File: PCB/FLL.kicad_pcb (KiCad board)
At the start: 2 copper layers, 9 parts, among them U1 MCP73831-2-MC, U3 LM317L_SOT-89

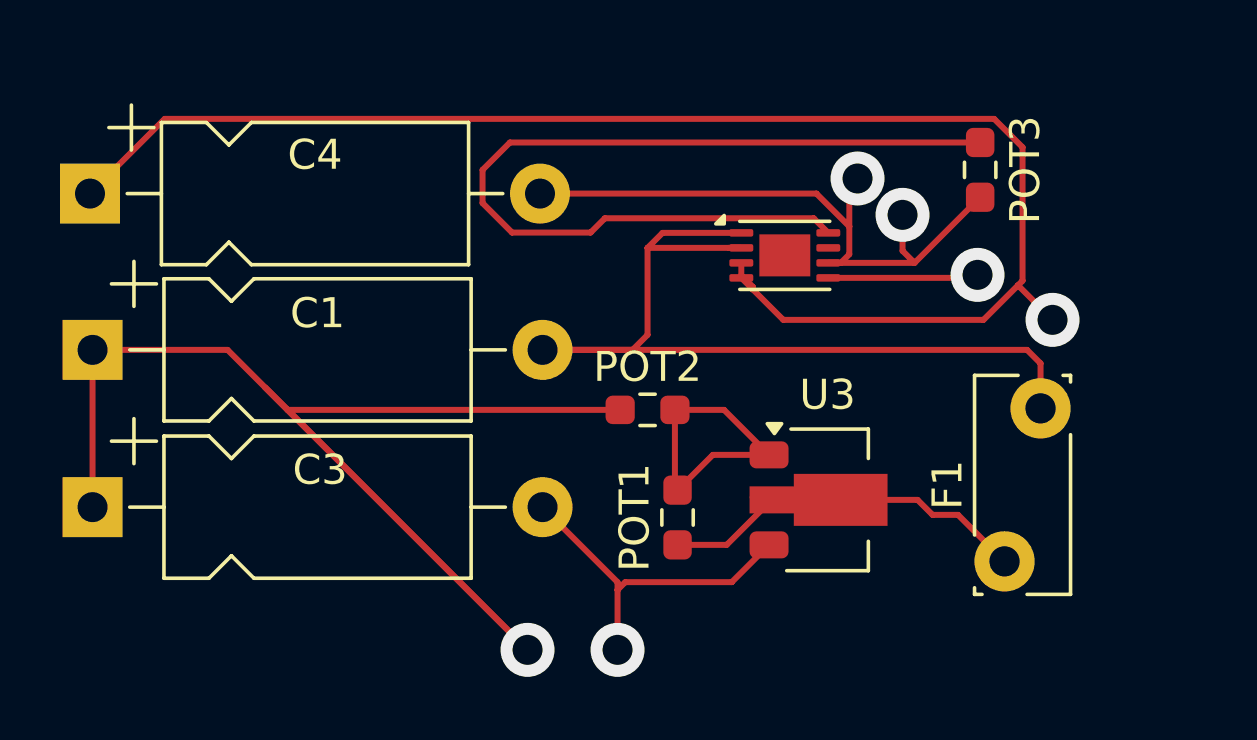
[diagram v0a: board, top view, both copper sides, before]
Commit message: Update PCB design configuration and net colors
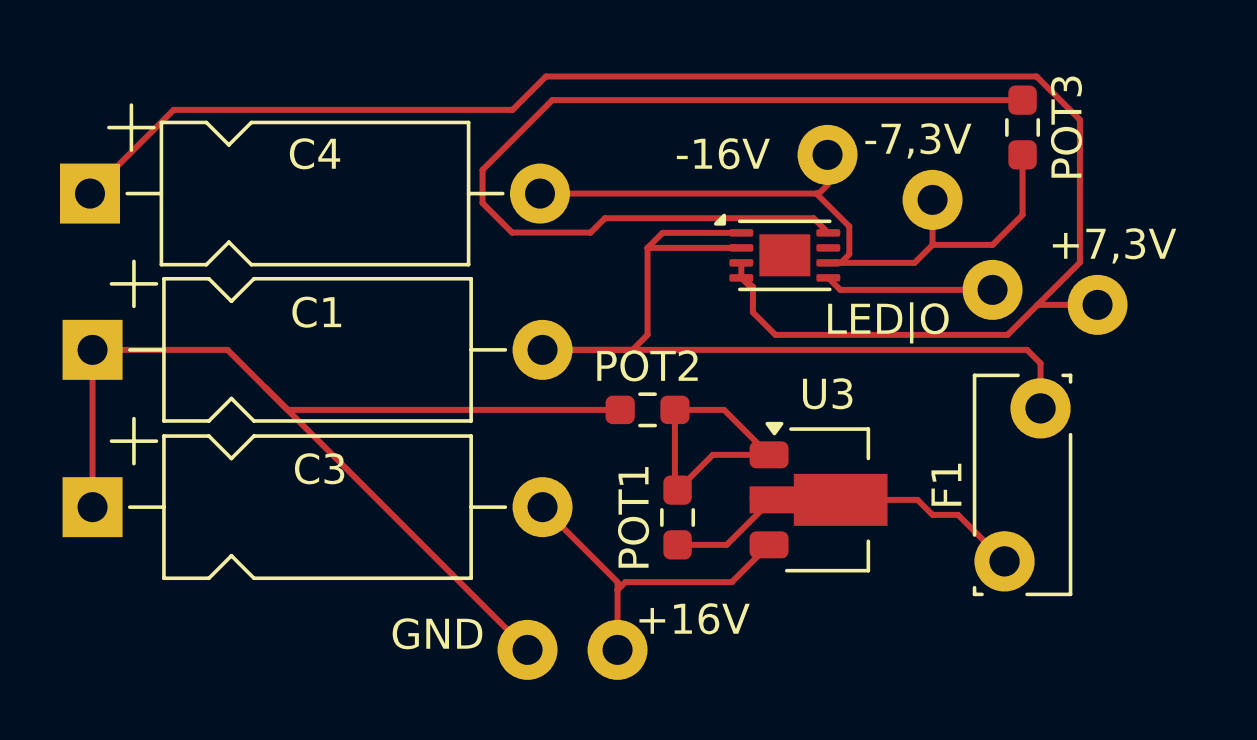
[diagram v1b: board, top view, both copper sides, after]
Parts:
- added ?: , , F.Cu at (170.5, 36.0)
- added ?: , , F.Cu at (160.5, 52.5)
- added ?: , , F.Cu at (176.0, 40.5)
- added ?: , , F.Cu at (163.5, 52.5)
- added ?: , , F.Cu at (174.0, 37.5)
- added ?: , , F.Cu at (179.5, 41.0)
- moved POT3 2.00 mm to (177.0, 35.1)
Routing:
- net GND: track 47.3 -> 36.0 mm, vias 1 -> 0
- net +7.5V: track 50.1 -> 56.5 mm, vias 1 -> 0
- net -16V: track 22.4 -> 25.1 mm, vias 2 -> 0
- net Net-(U1-PROG): track 30.4 -> 32.4 mm
- net +1V0: track 5.02 -> 5.78 mm, vias 1 -> 0
- net +16V: vias 1 -> 0
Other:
- board text added: "+16V"
- board text added: "+7,3V"
- board text added: "-16V"
- board text added: "-7,3V"
- board text added: "GND"
- board text added: "LED|O"

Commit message: chore: Update PCB design configuration and remove unnecessary files
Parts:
- added J1: Jack-DC, Connector_BarrelJack:BarrelJack_CUI_PJ-063AH_Horizontal_CircularHoles, F.Cu at (6.78, 2.52)
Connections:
- ? pad 1: -16V -> -7.5V
- C3 pad 2: +16V -> Net-(U3-VI)
- C4 pad 2: -16V -> -7.5V
- POT3 pad 2: -16V -> -7.5V
- U1 pad 6: -16V -> -7.5V
- U3 pad 3: +16V -> Net-(U3-VI)
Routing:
- net -16V: track 25.1 -> 1.50 mm
- net -7.5V: track 0.00 -> 23.1 mm
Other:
- board text added: "C4"
- board text removed: "${REFERENCE}"

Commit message: chore: Update PCB design configuration and remove unnecessary files
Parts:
- removed J1: Jack-DC, Connector_BarrelJack:BarrelJack_CUI_PJ-063AH_Horizontal_CircularHoles

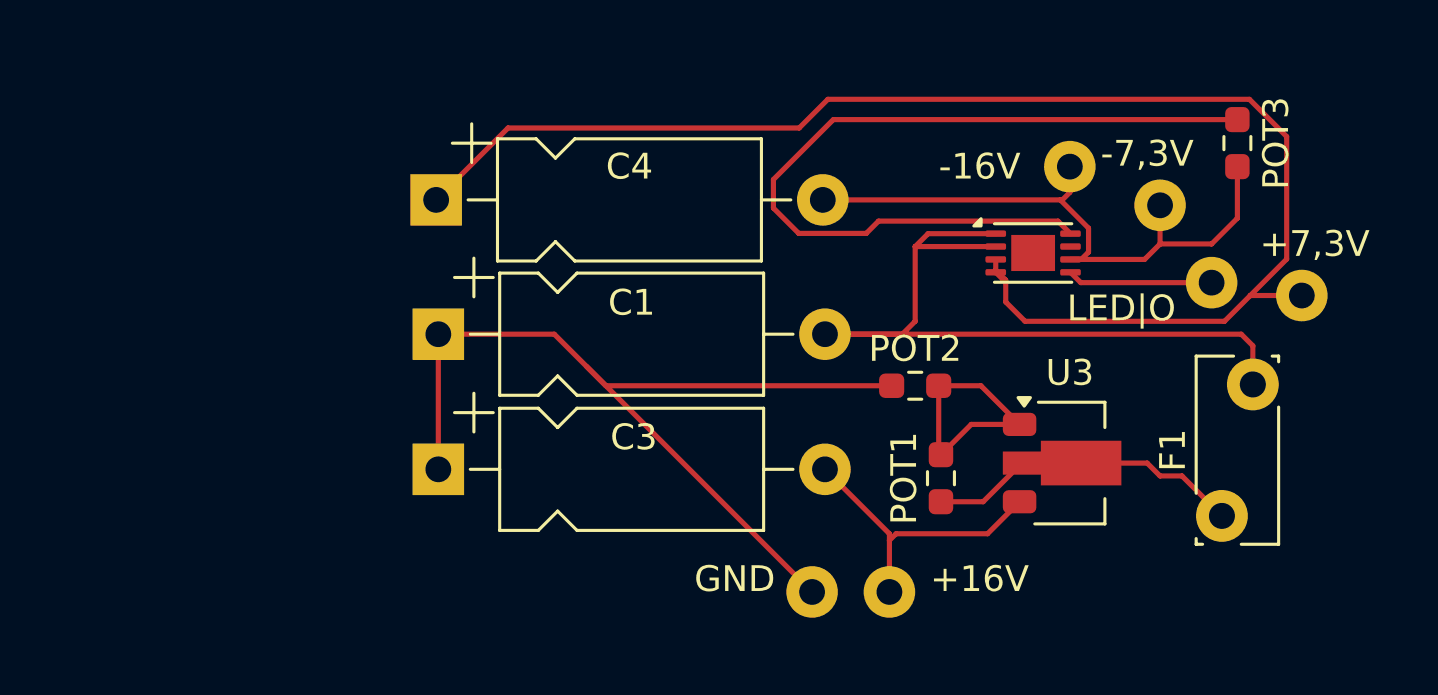
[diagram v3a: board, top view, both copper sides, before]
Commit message: Update PCB design configuration and remove unnecessary files
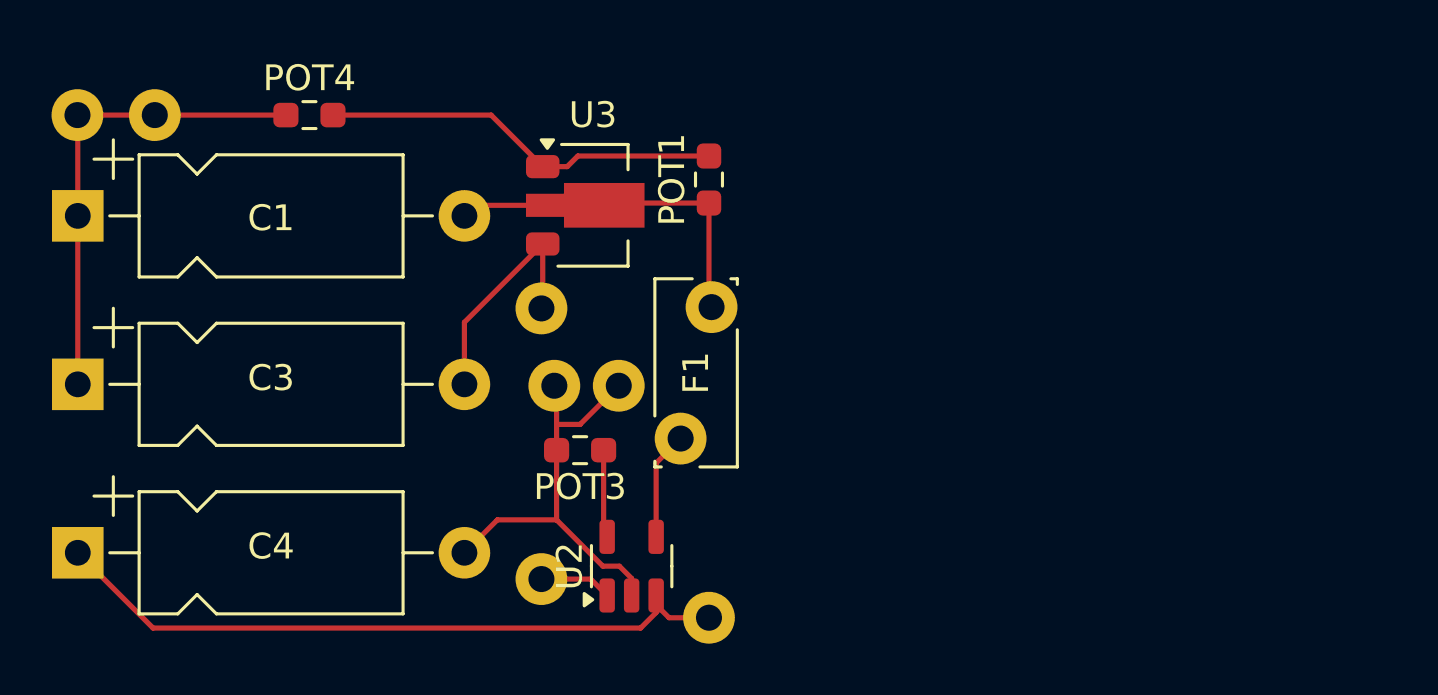
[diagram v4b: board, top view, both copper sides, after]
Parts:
- removed the ? at (170.5, 36.0)
- removed the ? at (160.5, 52.5)
- removed the ? at (176.0, 40.5)
- removed the ? at (163.5, 52.5)
- removed the ? at (174.0, 37.5)
- removed the ? at (179.5, 41.0)
- removed POT2: 1,4kΩ, Resistor_SMD:R_0603_1608Metric_Pad0.98x0.95mm_HandSolder
- removed U1: MCP73831-2-MC, Package_DFN_QFN:DFN-8-1EP_3x2mm_P0.5mm_EP1.7x1.4mm
- added ?: , , F.Cu at (135.0, 34.0)
- added ?: , , F.Cu at (153.0, 44.5)
- added ?: , , F.Cu at (150.5, 44.5)
- added ?: , , F.Cu at (150.0, 41.5)
- added ?: , , F.Cu at (132.0, 34.0)
- added ?: , , F.Cu at (150.0, 52.0)
- added ?: , , F.Cu at (156.5, 53.5)
- added POT4: 1,4kΩ, Resistor_SMD:R_0603_1608Metric_Pad0.98x0.95mm_HandSolder, F.Cu at (141.0, 34.0)
- added U2: MCP73831-2-OT, Package_TO_SOT_SMD:SOT-23-5, F.Cu at (153.5, 51.5)
- moved POT3 28.1 mm to (151.5, 47.0), turned to 180 degrees
- moved F1 21.4 mm to (156.6, 41.5), turned to -90 degrees
- moved U3 21.0 mm to (152.0, 37.5)
- moved C4 19.5 mm to (132.0, 51.0)
- moved C1 14.7 mm to (132.0, 37.9)
- moved POT1 14.7 mm to (156.5, 36.5)
- moved C3 14.4 mm to (132.0, 44.4)
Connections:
- C1 pad 2: Net-(C1-Pad2) -> Net-(U3-VO)
- F1 pad 2: Net-(C1-Pad2) -> Net-(U2-V_{DD})
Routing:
- net Net-(C1-Pad2): track 31.4 -> 0.00 mm
- net +7.5V: track 56.5 -> 27.2 mm
- net Net-(U2-PROG): track 32.4 -> 3.42 mm
- net GND: track 36.0 -> 18.6 mm
- net +16V: track 11.5 -> 0.00 mm
- net Net-(U3-VI): track 0.00 -> 9.22 mm
- net -7.5V: track 23.1 -> 17.4 mm
- net Net-(U3-ADJ): track 10.0 -> 15.6 mm
- net Net-(U2-V_{DD}): track 0.00 -> 4.21 mm
- net +1V0: track 5.64 -> 2.81 mm
- net -16V: track 1.50 -> 0.00 mm
- net Net-(U3-VO): track 12.4 -> 13.8 mm
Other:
- board text removed: "+16V"
- board text removed: "+7,3V"
- board text removed: "-16V"
- board text removed: "-7,3V"
- board text removed: "C4"
- board text removed: "GND"
- board text removed: "LED|O"

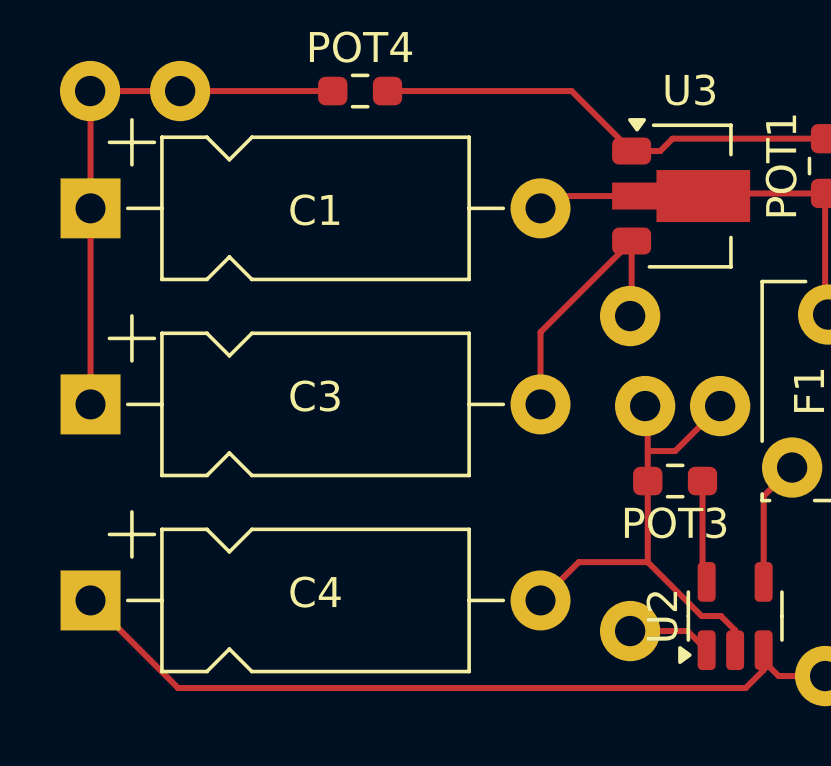
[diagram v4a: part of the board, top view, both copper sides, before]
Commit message: Update PCB design configuration and remove unnecessary files
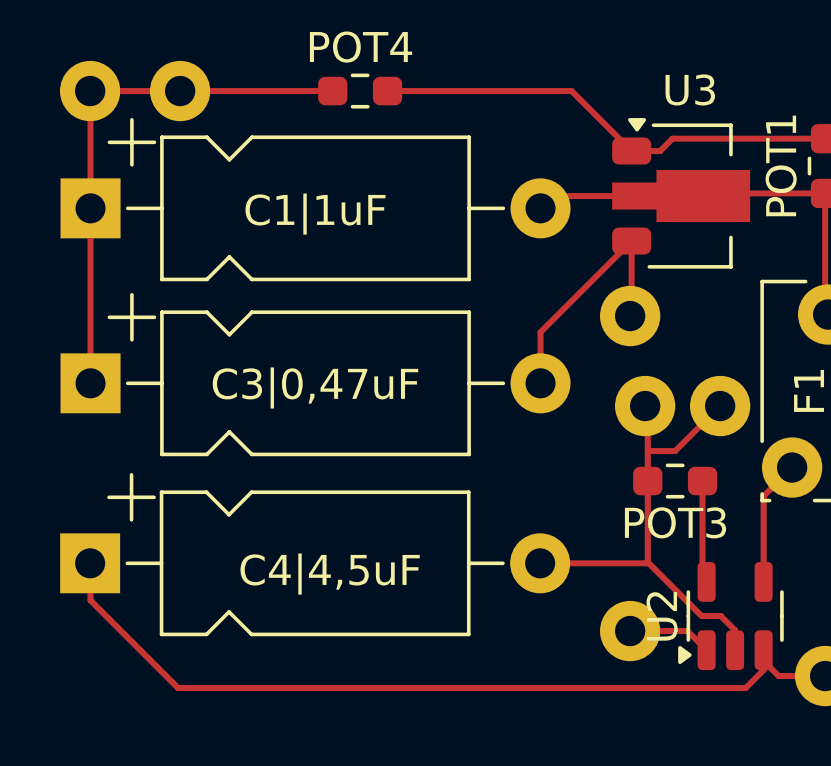
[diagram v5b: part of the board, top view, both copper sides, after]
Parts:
- moved C4|4,5uF 1.24 mm to (132.0, 49.7)
- moved C3|0,47uF 0.70 mm to (132.0, 43.7)
- renumbered C1 to C1|1uF, C3 to C3|0,47uF, C4 to C4|4,5uF
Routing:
- net +7.5V: track 27.2 -> 28.4 mm
- net -7.5V: track 17.4 -> 16.4 mm
- net Net-(U3-VI): track 9.22 -> 8.52 mm
- net GND: track 18.6 -> 17.9 mm
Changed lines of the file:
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@@
 	(footprint "Capacitor_THT:CP_Axial_L10.0mm_D4.5mm_P15.00mm_Horizontal"
 		(layer "F.Cu")
-		(at 132.0125 44.445)
+		(at 132.0125 43.7425)
 		(descr "CP, Axial series, Axial, Horizontal, pin pitch=15mm, , length*diameter=10*4.5mm^2, Electrolytic Capacitor, , http://www.vishay.com/docs/28325/021asm.pdf")
 		(tags "CP Axial series Axial Horizontal pin pitch 15mm  length 10mm diameter 4.5mm Electrolytic Capacitor")
-		(property "Reference" "C3"
-			(at 7.5 -0.2425 0)
+		(property "Reference" "C3|0,47uF"
+			(at 7.5 0.055 0)
 			(layer "F.SilkS")
 			(effects
@@
 			(at 7.9875 1.555 0)
 			(layer "F.Fab")
+			(hide yes)
 			(effects
 				(font
@@
 	(footprint "Capacitor_THT:CP_Axial_L10.0mm_D4.5mm_P15.00mm_Horizontal"
 		(layer "F.Cu")
-		(at 132.0125 50.98)
+		(at 132 49.7425)
 		(descr "CP, Axial series, Axial, Horizontal, pin pitch=15mm, , length*diameter=10*4.5mm^2, Electrolytic Capacitor, , http://www.vishay.com/docs/28325/021asm.pdf")
 		(tags "CP Axial series Axial Horizontal pin pitch 15mm  length 10mm diameter 4.5mm Electrolytic Capacitor")
-		(property "Reference" "C4"
-			(at 7.5 -0.2425 0)
+		(property "Reference" "C4|4,5uF"
+			(at 8 0.2575 0)
 			(layer "F.SilkS")
 			(effects
@@
 			(at 7.9875 1.52 0)
 			(layer "F.Fab")
+			(hide yes)
 			(effects
 				(font
@@
 			(layer "F.Fab")
 		)
-		(fp_text user "${REFERENCE}"
-			(at 7.5 0 0)
-			(layer "F.Fab")
-			(effects
-				(font
-					(size 1 1)
-					(thickness 0.15)
-				)
-			)
-		)
 		(pad "1" thru_hole rect
 			(at 0 0)
@@
 			(at 0 1.43 0)
 			(layer "F.Fab")
+			(hide yes)
 			(effects
 				(font
@@
 		)
 		(property "Value" "MCP73831-2-OT"
-			(at 0 2.4 90)
+			(at 3 5 90)
 			(layer "F.Fab")
+			(hide yes)
 			(effects
 				(font
@@
 		(descr "CP, Axial series, Axial, Horizontal, pin pitch=15mm, , length*diameter=10*4.5mm^2, Electrolytic Capacitor, , http://www.vishay.com/docs/28325/021asm.pdf")
 		(tags "CP Axial series Axial Horizontal pin pitch 15mm  length 10mm diameter 4.5mm Electrolytic Capacitor")
-		(property "Reference" "C1"
+		(property "Reference" "C1|1uF"
 			(at 7.5 0.09 0)
 			(layer "F.SilkS")
@@
 			(at 7.5 1.59 0)
 			(layer "F.Fab")
+			(hide yes)
 			(effects
 				(font
@@
 		)
 		(fp_text user "${REFERENCE}"
-			(at 7.5 0 0)
+			(at 7.4875 0.09 0)
 			(layer "F.Fab")
 			(effects
@@
 	)
 	(segment
-		(start 154.45 52.6375)
-		(end 154.45 53)
+		(start 132.0125 50.98)
+		(end 134.9325 53.9)
 		(width 0.2)
 		(layer "F.Cu")
@@
 	)
 	(segment
-		(start 132.0125 50.98)
-		(end 134.9325 53.9)
+		(start 132.0125 49.7425)
+		(end 132.0125 50.98)
+		(width 0.2)
+		(layer "F.Cu")
+		(net 1)
+	)
+	(segment
+		(start 154.45 52.6375)
+		(end 154.45 53)
 		(width 0.2)
 		(layer "F.Cu")
@@
 	)
 	(segment
-		(start 132.0875 37.835)
-		(end 132.0125 37.91)
+		(start 132.0125 37.91)
+		(end 132.0125 43.7425)
 		(width 0.2)
 		(layer "F.Cu")
@@
 	)
 	(segment
-		(start 132.0125 34.0125)
-		(end 132 34)
+		(start 132.0875 37.835)
+		(end 132.0125 37.91)
 		(width 0.2)
 		(layer "F.Cu")
@@
 	)
 	(segment
-		(start 132.0125 37.91)
-		(end 132.0125 44.445)
+		(start 132.0125 34.0125)
+		(end 132 34)
 		(width 0.2)
 		(layer "F.Cu")
@@
 	)
 	(segment
-		(start 147.0125 44.445)
-		(end 147.0125 42.0375)
+		(start 150.05 41.45)
+		(end 150 41.5)
 		(width 0.2)
 		(layer "F.Cu")
@@
 	)
 	(segment
-		(start 150.05 41.45)
-		(end 150 41.5)
+		(start 147.0125 43.7425)
+		(end 147.0125 42.0375)
 		(width 0.2)
 		(layer "F.Cu")
@@
 	)
 	(segment
-		(start 150.5875 49.703052)
-		(end 148.289448 49.703052)
-		(width 0.2)
-		(layer "F.Cu")
-		(net 7)
-	)
-	(segment
 		(start 152.384448 51.5)
 		(end 150.5875 49.703052)
@@
 	)
 	(segment
-		(start 147.3575 51.325)
-		(end 147.0125 50.98)
+		(start 150.5875 47)
+		(end 150.5875 49.703052)
 		(width 0.2)
 		(layer "F.Cu")
@@
 	)
 	(segment
-		(start 150.5875 47)
-		(end 150.5875 49.703052)
+		(start 153.5 51.975001)
+		(end 153.024999 51.5)
 		(width 0.2)
 		(layer "F.Cu")
@@
 	)
 	(segment
-		(start 153.5 51.975001)
-		(end 153.024999 51.5)
+		(start 147.0125 49.7425)
+		(end 150.548052 49.7425)
 		(width 0.2)
 		(layer "F.Cu")
@@
 	)
 	(segment
-		(start 153.024999 51.5)
-		(end 152.384448 51.5)
+		(start 150.548052 49.7425)
+		(end 150.5875 49.703052)
 		(width 0.2)
 		(layer "F.Cu")
@@
 	)
 	(segment
-		(start 150.5 44.5)
-		(end 150.5 45)
+		(start 153.024999 51.5)
+		(end 152.384448 51.5)
 		(width 0.2)
 		(layer "F.Cu")
@@
 	)
 	(segment
-		(start 148.289448 49.703052)
-		(end 147.0125 50.98)
+		(start 150.5 44.5)
+		(end 150.5 45)
 		(width 0.2)
 		(layer "F.Cu")
